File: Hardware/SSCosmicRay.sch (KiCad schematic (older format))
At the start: 0 parts

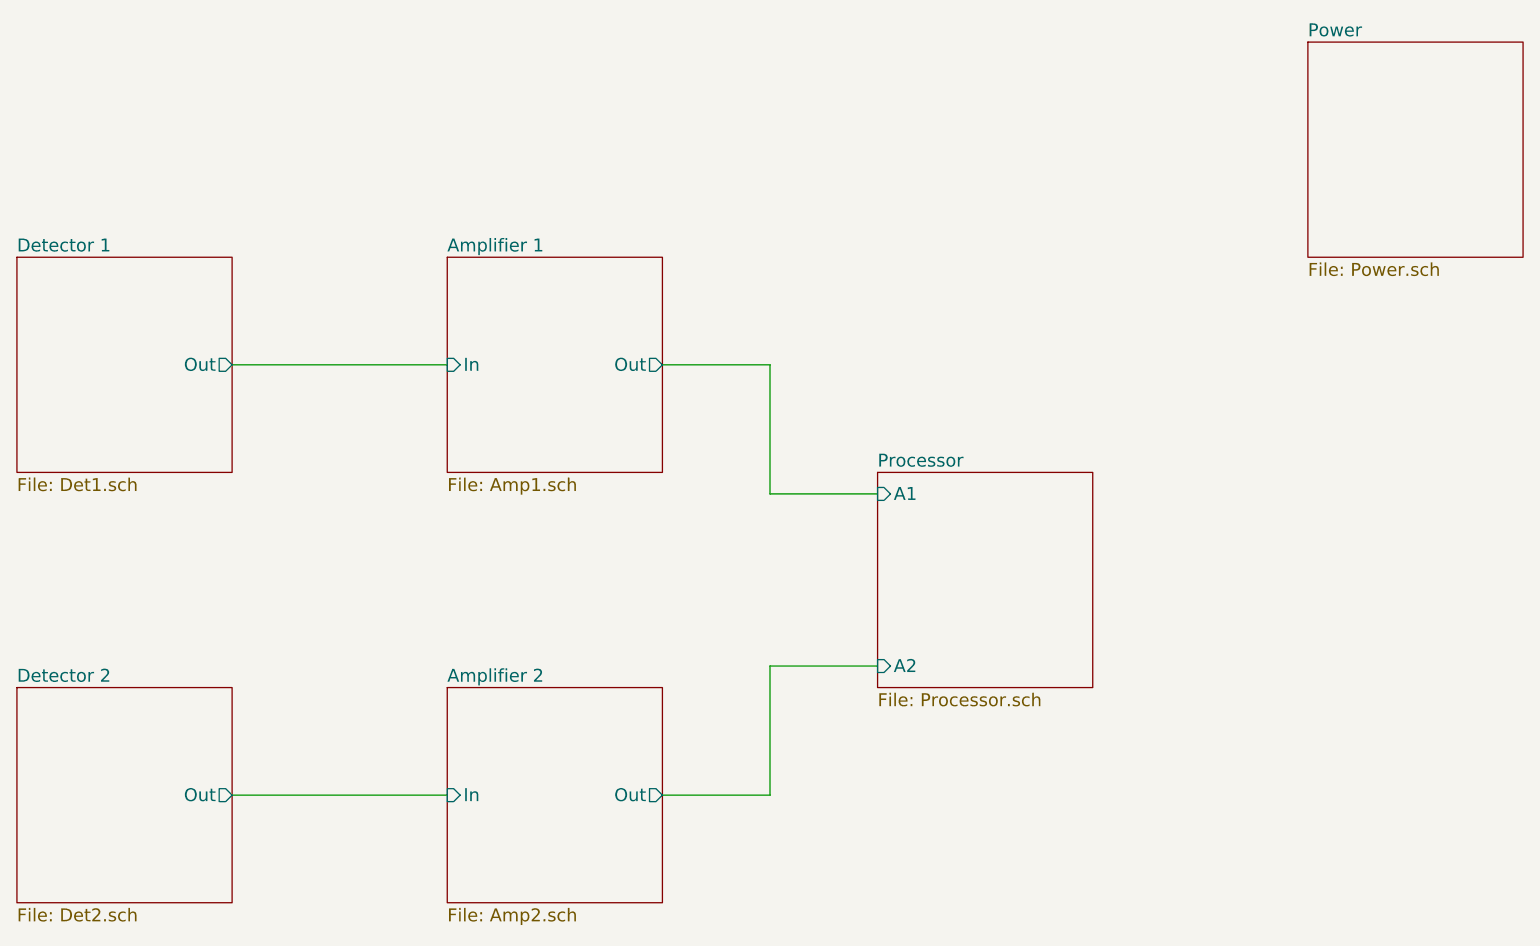
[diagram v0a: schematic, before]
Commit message: Move amplifiers into detection subsheets
Reannotate
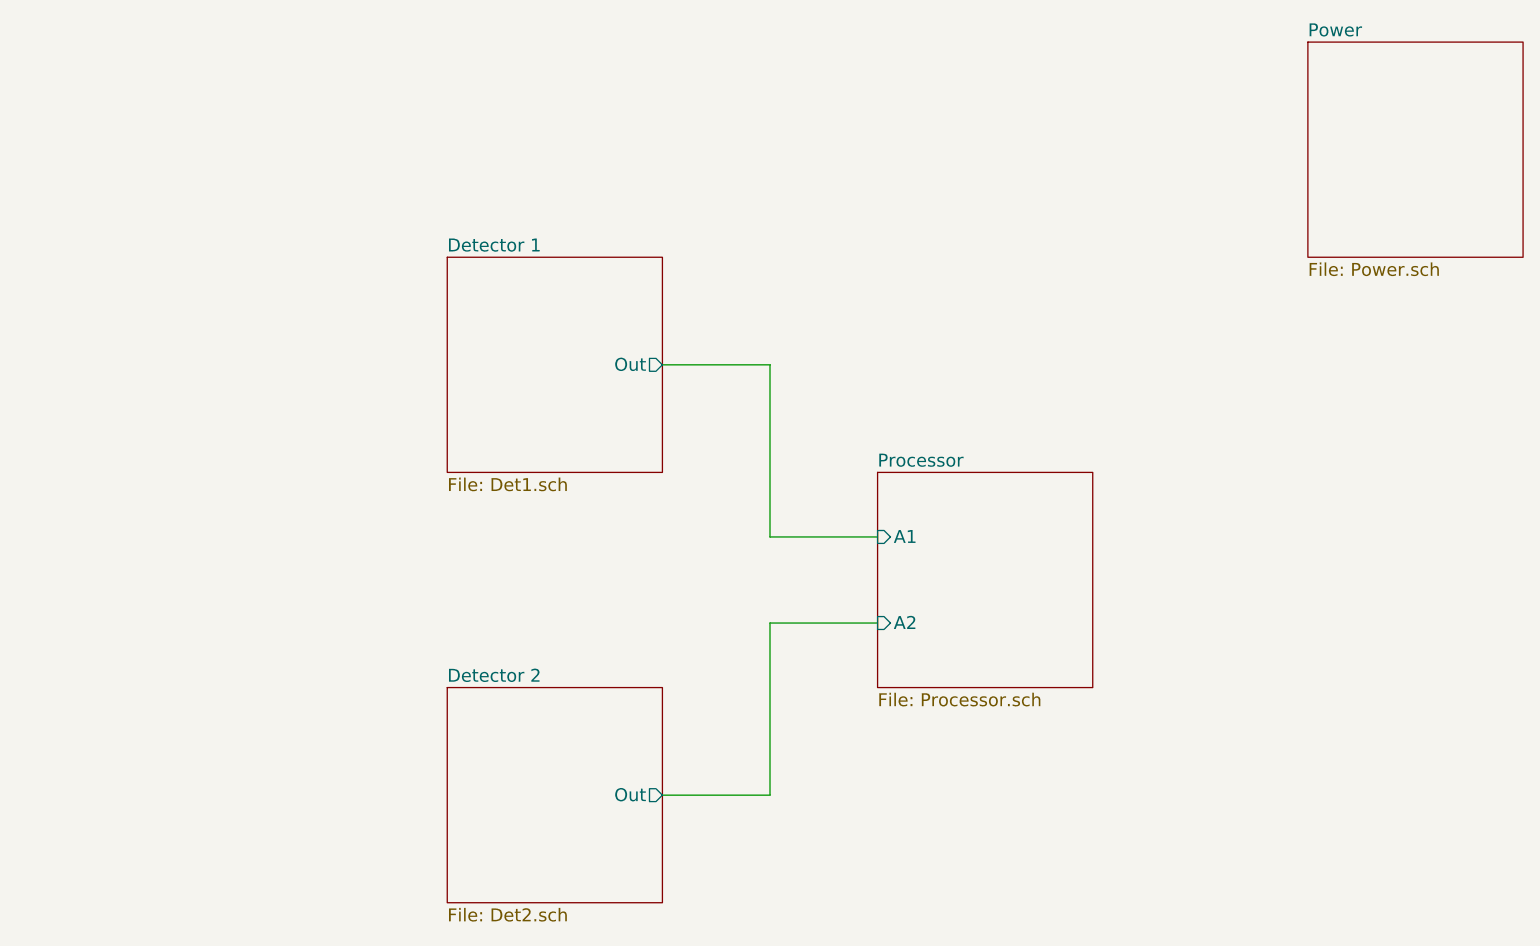
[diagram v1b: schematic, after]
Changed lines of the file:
@@
 $Descr A4 11693 8268
 encoding utf-8
-Sheet 1 7
+Sheet 1 5
 Title "Solid State Cosmic Ray Detector"
 Date "24 dec 2013"
@@
 $EndDescr
 $Sheet
-S 2400 2400 1000 1000
+S 4400 2400 1000 1000
 U 523CFD04
 F0 "Detector 1" 60
 F1 "Det1.sch" 60
-F2 "Out" O R 3400 2900 60
+F2 "Out" O R 5400 2900 60
 $EndSheet
-$Sheet
-S 4400 2400 1000 1000
-U 523CFD69
-F0 "Amplifier 1" 60
-F1 "Amp1.sch" 60
-F2 "Out" O R 5400 2900 60
-F3 "In" I L 4400 2900 60
-$EndSheet
-Wire Wire Line
-	3400 2900 4400 2900
 Wire Wire Line
 	5400 2900 5900 2900
@@
 F0 "Processor" 60
 F1 "Processor.sch" 60
-F2 "A1" I L 6400 3500 60
-F3 "A2" I L 6400 4300 60
+F2 "A1" I L 6400 3700 60
+F3 "A2" I L 6400 4100 60
 $EndSheet
 Wire Wire Line
-	5900 2900 5900 3500
+	5900 2900 5900 3700
 Wire Wire Line
-	5900 3500 6400 3500
+	5900 3700 6400 3700
 $Sheet
 S 4400 4400 1000 1000
-U 52414C52
-F0 "Amplifier 2" 60
-F1 "Amp2.sch" 60
-F2 "Out" O R 5400 4900 60
-F3 "In" I L 4400 4900 60
-$EndSheet
-$Sheet
-S 2400 4400 1000 1000
 U 52414C7B
 F0 "Detector 2" 60
 F1 "Det2.sch" 60
-F2 "Out" O R 3400 4900 60
+F2 "Out" O R 5400 4900 60
 $EndSheet
-Wire Wire Line
-	3400 4900 4400 4900
 Wire Wire Line
 	5400 4900 5900 4900
 Wire Wire Line
-	5900 4900 5900 4300
+	5900 4900 5900 4100
 Wire Wire Line
-	5900 4300 6400 4300
+	5900 4100 6400 4100
 $Sheet
 S 8400 1400 1000 1000
